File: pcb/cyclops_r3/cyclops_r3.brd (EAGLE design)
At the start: 68.6 x 53.3 mm, 47 parts, among them IC1 317-N, IC5 LM324, Q1 SUM11006, U1 ADR03, U2 OP1177

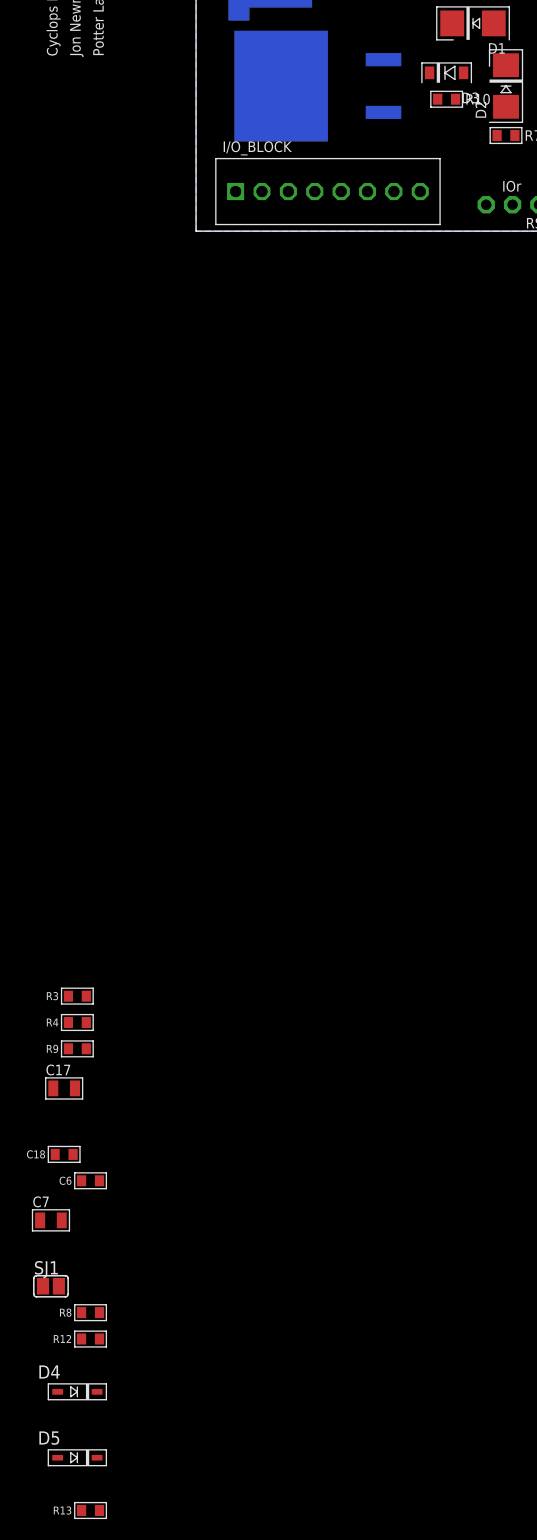
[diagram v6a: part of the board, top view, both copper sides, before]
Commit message: Improved input diode clamp.
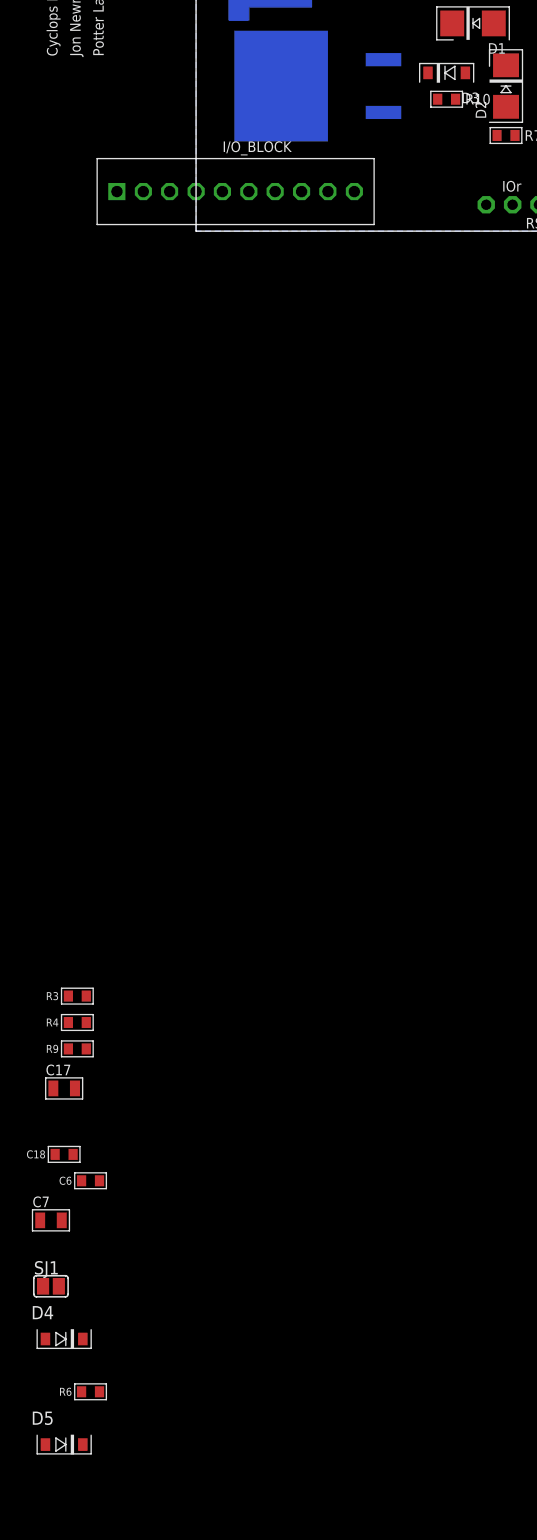
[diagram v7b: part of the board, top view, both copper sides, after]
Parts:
- removed R12, R8: 1k, cyclops:0603
- removed R13: 10k, cyclops:0603
- added R6: 1k, cyclops:0603
- CTL_K: value 10k -> 1k
- D4, D5: value 1N4148WS -> DS11015; device cyclops:SOD-323F -> cyclops:SOD123
- I/O_BLOCK: value SCREW8 -> SCREW10_0.1-THRU; device cyclops:SCREW8 -> cyclops:SCREW10
- IC5: value LM324 -> LM324N
- moved D4 5.24 mm to (-12.7, -106.7)
- moved D5 1.80 mm to (-12.7, -116.8)
- renumbered CURR/OPT to CURR/AUX
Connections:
- removed net BUFTEMP: I/O_BLOCK.P$8, U2.2, U2.6
- removed net N$5: D4.A, R12.2, R8.2
- new net VTEMP: I/O_BLOCK.P$9, U2.2, U2.6
- new net _VIN: D4.C, D5.A, IC5.10, IC5.3, R6.2
- net +12V: now also D5.C; no longer R12.1
- net GND: now also D4.A, I/O_BLOCK.P$10; no longer D4.C, R13.2
- net N$7: now also R6.1; no longer D5.A, R8.1
- net VAUX: now also I/O_BLOCK.P$8; no longer I/O_BLOCK.P$7
- net VI: now also I/O_BLOCK.P$7; no longer I/O_BLOCK.P$6
- net VIN: now also I/O_BLOCK.P$5
- net VREF: now also I/O_BLOCK.P$6; no longer D5.C, I/O_BLOCK.P$5, IC5.10, IC5.3, R13.1

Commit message: Almost finished. Still trying to understand the best N-Channel MOSFET for sinking LED current.
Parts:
- removed CURR/AUX: (no value), HOSS:A_TOGGLE_SPST
- added R8: 220k, cyclops:0603
- added S2: CURR/AUX, cyclops:PCM12
- added S3: TEST, cyclops:CFPA
- CTL_K: device HOSS:RJ6S -> cyclops:SM-42/43A
- REF_ADJ: device cyclops:SM-42/43W -> cyclops:SM-42/43A
- moved C17 117.7 mm to (-26.7, 34.3)
- moved C18 117.7 mm to (-26.7, 27.9)
- moved C6 117.7 mm to (-24.1, 25.4)
- moved C7 117.7 mm to (-27.9, 21.6)
- moved D4 117.7 mm to (-26.7, 10.2)
- moved D5 117.7 mm to (-26.7, 0.00)
- moved R4 117.7 mm to (-25.4, 40.6)
- moved R6 117.7 mm to (-24.1, 5.08)
- moved R9 117.7 mm to (-25.4, 38.1)
- moved SJ1 109.2 mm to (-15.2, 7.62)
- moved CTL_K 104.4 mm to (16.8, 2.86)
- moved R3 75.1 mm to (-16.5, 1.27)
- moved I/O_BLOCK 20.3 mm to (3.81, 24.1), turned to 90 degrees
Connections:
- net _VIN renamed _VREF
- removed net LED+: I/O_BLOCK.P$3
- new net VCTL: CTL_K.1, S3.2
- net +12V: now also I/O_BLOCK.P$3
- net DACA: now also S3.3
- net GND: now also CTL_K.3, R8.1; no longer CTL_K.E
- net N$3: now also R8.2
- net N$7: now also CTL_K.2; no longer CTL_K.S
- net VAUX: now also S2.3; no longer CURR/AUX.P$3
- net VFB: now also S2.2; no longer CURR/AUX.P$2
- net VI: now also S2.1, S3.1; no longer CURR/AUX.P$1
- net VIN: no longer CTL_K.A
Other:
- board text removed: "CURR"
- board text removed: "OPT"
